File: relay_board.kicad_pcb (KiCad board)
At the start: 2 copper layers, 23 parts, among them J1 Conn_01x09_Male, J2 Conn_01x10_Male, J3 Conn_01x10_Male, K1 G5Q-1A, K2 G5Q-1A, K3 G5Q-1A, K4 G5LE-1, K5 G5LE-1, K6 G5Q-1A, K7 G5Q-1A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

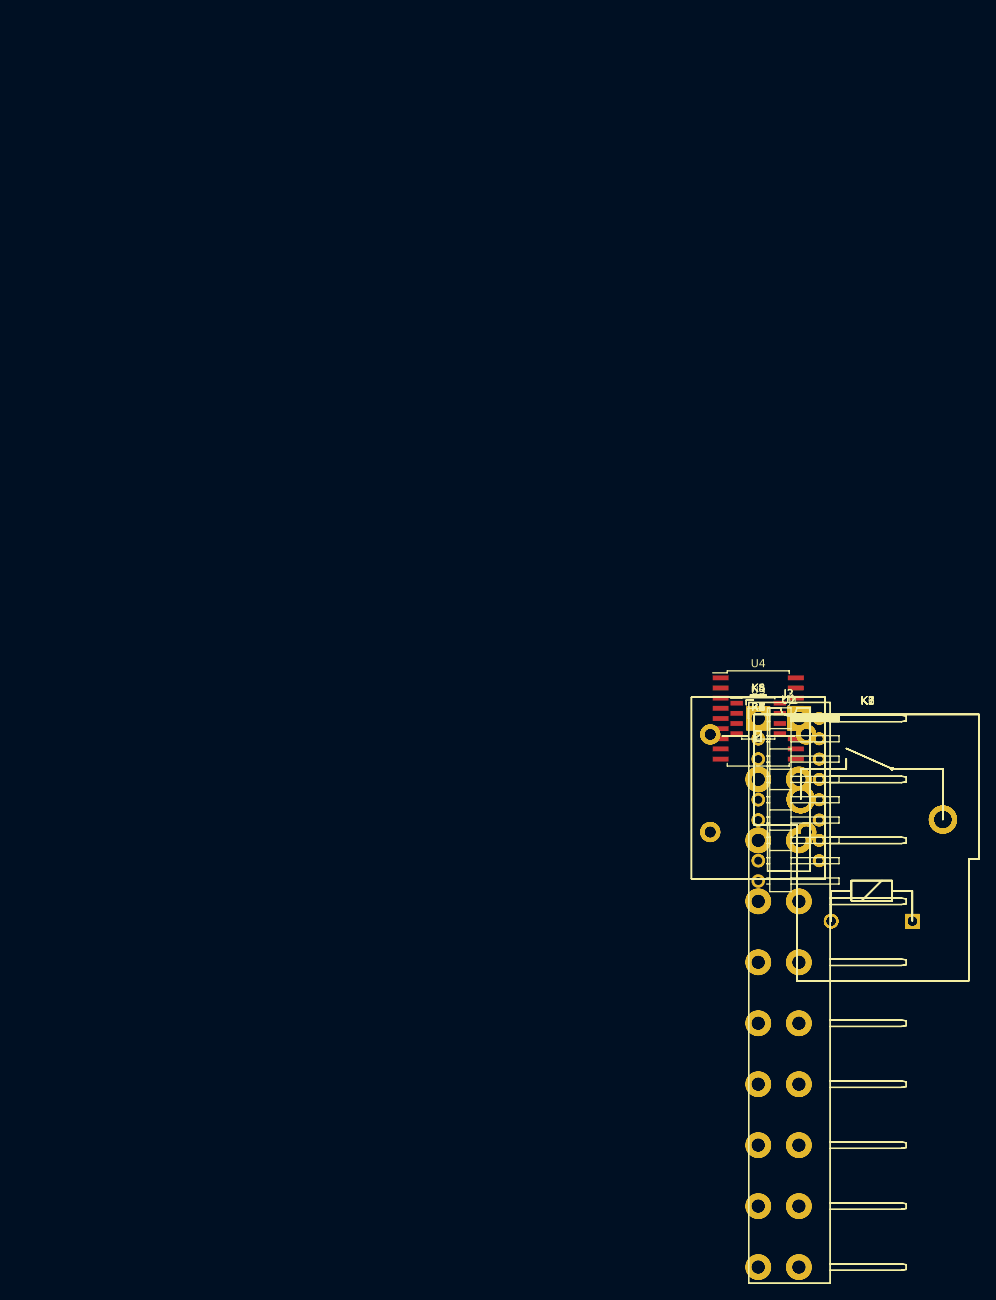
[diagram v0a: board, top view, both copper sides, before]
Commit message: Routed relay board, without finishing.
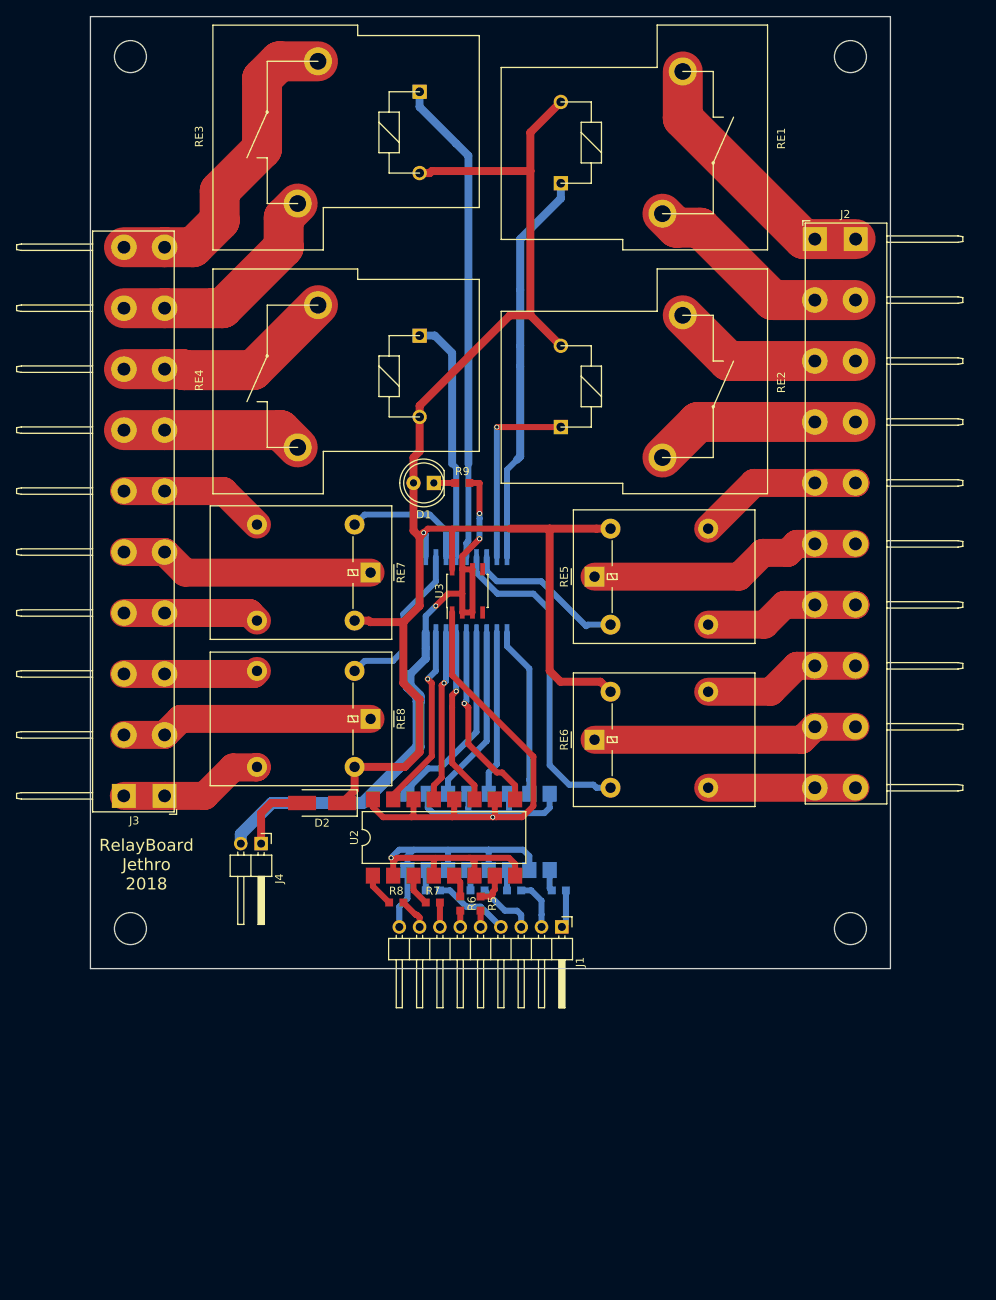
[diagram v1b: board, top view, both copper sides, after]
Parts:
- removed K1, K2, K3, K6, K7: G5Q-1A, Relay_THT:Relay_SPST_Hongfa_HF105F1
- removed K4, K5, K8: G5LE-1, Relay_THT:Relay_SPDT_Omron-G5LE-1
- added D1: LED, LED_THT:LED_D5.0mm, F.Cu at (108.0, 75.6)
- added D2: D_Schottky, Diode_SMD:D_SMA_Handsoldering, F.Cu at (94.0, 115.6)
- added J4: Conn_01x02_Male, Connector_PinHeader_2.54mm:PinHeader_1x02_P2.54mm_Horizontal, F.Cu at (86.4, 120.7)
- added R9: R, Resistor_SMD:R_0603_1608Metric_Pad0.99x1.00mm_HandSolder, F.Cu at (111.5, 75.6)
- added RE1: G5Q-1A, Relay_THT:Relay_SPST_Hongfa_HF105F1, F.Cu at (149.2, 18.8)
- added RE2: G5Q-1A, Relay_THT:Relay_SPST_Hongfa_HF105F1, F.Cu at (149.2, 49.3)
- added RE3: G5Q-1A, Relay_THT:Relay_SPST_Hongfa_HF105F1, F.Cu at (80.8, 45.9)
- added RE4: G5Q-1A, Relay_THT:Relay_SPST_Hongfa_HF105F1, F.Cu at (80.8, 76.4)
- added RE5: G5LE-1, Relay_THT:Relay_SPDT_Omron-G5LE-1, F.Cu at (128.0, 87.3)
- added RE6: G5LE-1, Relay_THT:Relay_SPDT_Omron-G5LE-1, F.Cu at (128.0, 107.7)
- added RE7: G5LE-1, Relay_THT:Relay_SPDT_Omron-G5LE-1, F.Cu at (100.0, 86.8)
- added RE8: G5LE-1, Relay_THT:Relay_SPDT_Omron-G5LE-1, F.Cu at (100.0, 105.1)
- R1, R2, R3, R4, U4: moved to B.Cu
- U1: footprint Package_DIP:DIP-16_W7.62mm -> Package_DIP:SMDIP-16_W9.53mm; moved to B.Cu
- U2: footprint Package_DIP:DIP-16_W7.62mm -> Package_DIP:SMDIP-16_W9.53mm
- moved J3 74.8 mm to (74.3, 114.7), turned to 180 degrees
- moved J2 60.3 mm to (155.6, 45.1)
- moved R8 50.8 mm to (103.3, 128.0)
- moved R7 46.7 mm to (107.8, 128.0)
- moved R4 46.0 mm to (107.8, 126.5)
- moved R6 43.9 mm to (111.3, 128.1), turned to 270 degrees
- moved U2 42.0 mm to (109.2, 119.9), turned to 90 degrees
- moved R5 41.7 mm to (113.8, 128.1), turned to 270 degrees
- moved R3 41.1 mm to (113.4, 126.5)
- moved U3 39.7 mm to (112.1, 89.1), turned to 90 degrees
- moved U4 39.6 mm to (112.0, 89.5), turned to 90 degrees
- moved U1 37.7 mm to (113.5, 119.2), turned to 90 degrees
- moved R2 37.3 mm to (118.0, 126.5)
- moved J1 35.8 mm to (124.0, 131.1), turned to 270 degrees
- moved R1 32.9 mm to (123.6, 126.5)
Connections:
- J2 pad 1: Net-(J2-Pad1) -> /R1NO
- J2 pad 10: Net-(J2-Pad10) -> /R6NO
- J2 pad 2: Net-(J2-Pad2) -> /R1IN
- J2 pad 3: Net-(J2-Pad3) -> /R2IN
- J2 pad 4: Net-(J2-Pad4) -> /R2NO
- J2 pad 5: Net-(J2-Pad5) -> /R5NC
- J2 pad 6: Net-(J2-Pad6) -> /R5IN
- J2 pad 7: Net-(J2-Pad7) -> /R5NO
- J2 pad 8: Net-(J2-Pad8) -> /R6NC
- J2 pad 9: Net-(J2-Pad9) -> /R6IN
- J3 pad 1: Net-(J3-Pad1) -> /R8NC
- J3 pad 10: Net-(J3-Pad10) -> /R3NO
- J3 pad 2: Net-(J3-Pad2) -> /R8IN
- J3 pad 3: Net-(J3-Pad3) -> /R8NO
- J3 pad 4: Net-(J3-Pad4) -> /R7NC
- J3 pad 5: Net-(J3-Pad5) -> /R7IN
- J3 pad 6: Net-(J3-Pad6) -> /R7NO
- J3 pad 7: Net-(J3-Pad7) -> /R4IN
- J3 pad 8: Net-(J3-Pad8) -> /R4NO
- J3 pad 9: Net-(J3-Pad9) -> /R3IN
- U2 pad 1: Net-(R5-Pad1) -> Net-(R8-Pad1)
- U2 pad 3: Net-(R6-Pad1) -> Net-(R7-Pad1)
- U2 pad 5: Net-(R7-Pad1) -> Net-(R6-Pad1)
- U2 pad 7: Net-(R8-Pad1) -> Net-(R5-Pad1)
- U4 pad 5: Net-(U2-Pad15) -> Net-(U2-Pad9)
- U4 pad 6: Net-(U2-Pad13) -> Net-(U2-Pad11)
- U4 pad 7: Net-(U2-Pad11) -> Net-(U2-Pad13)
- U4 pad 8: Net-(U2-Pad9) -> Net-(U2-Pad15)
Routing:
- net +12V: track 0.00 -> 190.9 mm, vias 0 -> 1
- net +5VP: track 0.00 -> 82.1 mm, vias 0 -> 1
- net GND: track 0.00 -> 77.7 mm, vias 0 -> 3
- net Net-(RE3-Pad1): track 0.00 -> 60.8 mm
- net GNDD: track 0.00 -> 59.8 mm, vias 0 -> 1
- net Net-(RE1-Pad1): track 0.00 -> 49.5 mm
- net Net-(RE6-Pad2): track 0.00 -> 41.2 mm
- net /R3NO: track 0.00 -> 41.2 mm
- net /R5IN: track 0.00 -> 34.3 mm
- net /R1NO: track 0.00 -> 33.7 mm
- net /R6IN: track 0.00 -> 33.3 mm
- net /R7IN: track 0.00 -> 31.9 mm
- net /R8IN: track 0.00 -> 31.7 mm
- net Net-(RE4-Pad1): track 0.00 -> 30.7 mm
- net /R3IN: track 0.00 -> 29.3 mm
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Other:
- board outline added: 100 x 119 mm
- net class 240V/10A added: clearance 3, trace_width 3.5, via_dia 2.5, via_drill 2
- net class 240V/20A added: clearance 3, trace_width 5, via_dia 3, via_drill 2.5
- net class Default: clearance 0.2 -> 0.3; trace_width 0.25 -> 1
- rule trace_clearance: 0.2 -> 0.3
- board text added: "RelayBoard Jethro 2018"

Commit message: Finished board.
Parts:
- moved J4 2.55 mm to (88.9, 120.4)
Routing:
- net /R3NO: track 41.2 -> 82.6 mm
- net /R5IN: track 34.3 -> 68.6 mm
- net /R1NO: track 33.7 -> 67.4 mm
- net /R6IN: track 33.3 -> 66.6 mm
- net /R7IN: track 31.9 -> 63.8 mm
- net /R8IN: track 31.7 -> 63.3 mm
- net /R1IN: track 28.6 -> 58.1 mm
- net /R3IN: track 29.3 -> 58.6 mm
- net /R4NO: track 27.7 -> 55.4 mm
- net /R2NO: track 26.0 -> 52.0 mm
- net /R2IN: track 24.0 -> 47.9 mm
- net /R4IN: track 22.6 -> 45.2 mm
- net /R5NC: track 25.9 -> 46.6 mm
- net /R6NC: track 19.8 -> 39.5 mm
- net /R5NO: track 24.5 -> 44.0 mm
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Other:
- outline, holes or cut-outs redrawn
- net class 240V/10A: clearance 3 -> 2
- net class 240V/20A: clearance 3 -> 2
- board text added: "+12V"
- board text added: "COM"
- board text added: "DANGER HIGH VOLTAGE"
- board text added: "GND"
- board text added: "NC"
- board text added: "NO"
- board text added: "Re1-15A"
- board text added: "Re2-15A"
- board text added: "Re3-15A"
- board text added: "Re4-15A"
- board text added: "Re5-10A"
- board text added: "Re6-10A"
- board text added: "Re7-10A"
- board text added: "Re8-10A"
- board text added: "Relay power"
